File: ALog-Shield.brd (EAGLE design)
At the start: 53.3 x 78.5 mm, 29 parts, among them U1 DS3231MZ/V+T

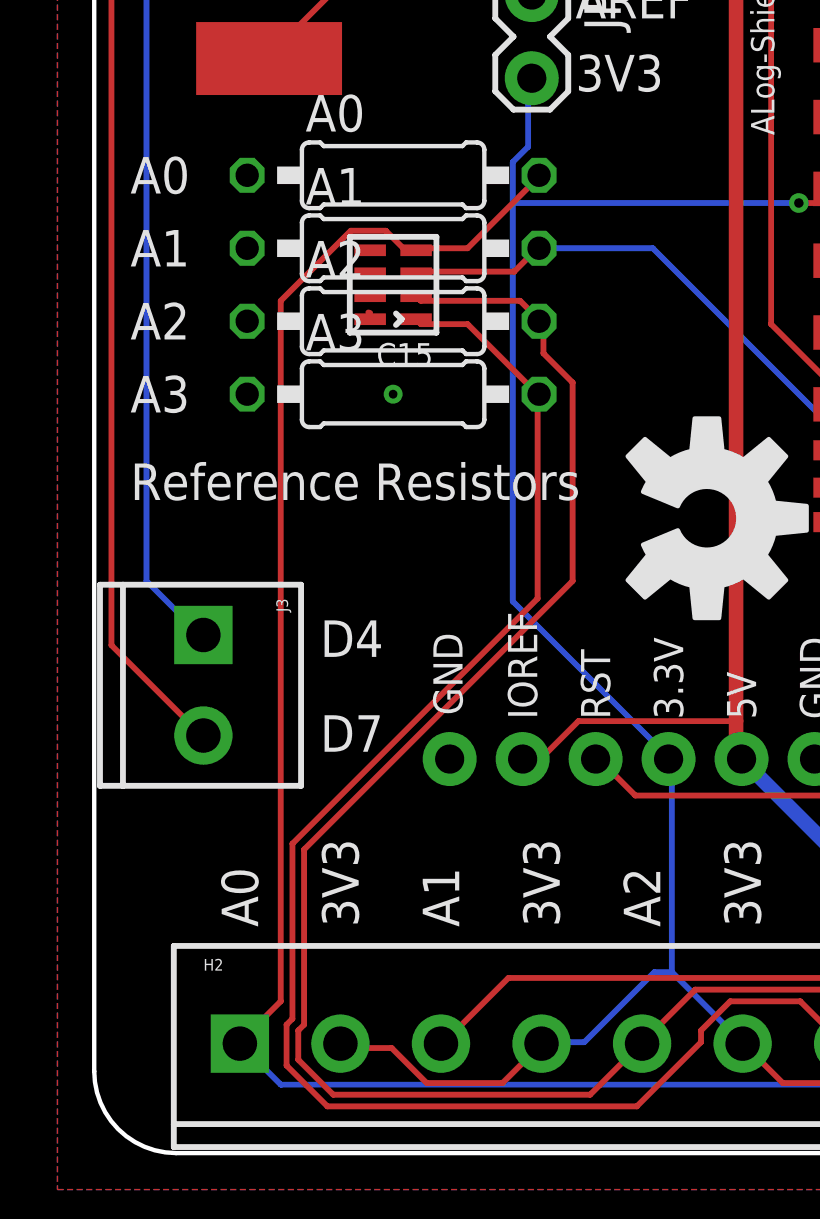
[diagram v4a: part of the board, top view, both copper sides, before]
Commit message: rm cap array
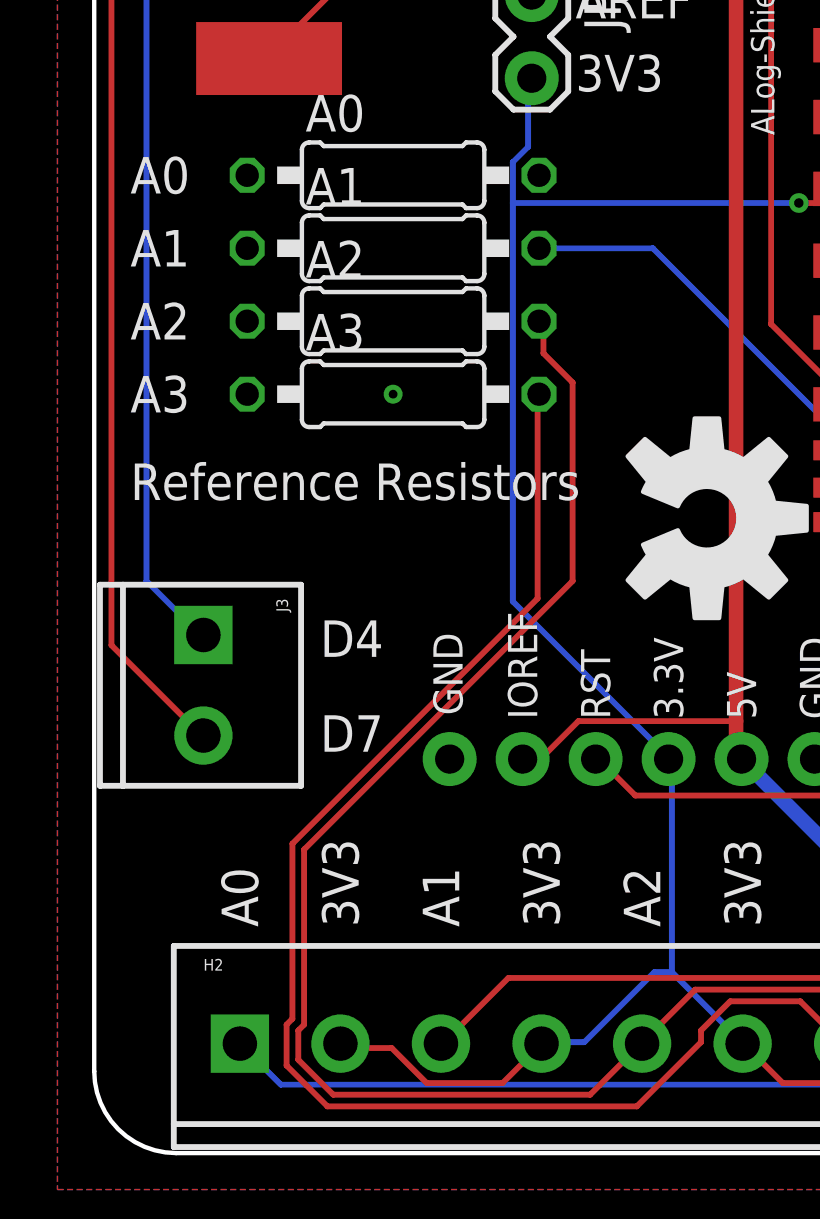
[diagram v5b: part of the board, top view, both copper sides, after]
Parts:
- removed C15: 10nF, rc-master-smd:CECJ-CTS-031817
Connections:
- net A0: no longer C15.D1
- net A1: no longer C15.C1
- net A2: no longer C15.B1
- net A3: no longer C15.A1
- net GND: no longer C15.A2, C15.B2, C15.C2, C15.D2
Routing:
- net A0: track 79.3 -> 41.4 mm
- net A3: track 75.5 -> 70.2 mm
- net A2: track 73.4 -> 68.7 mm
- net A1: track 64.1 -> 59.5 mm
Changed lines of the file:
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@@
 <attribute name="SF_ID" value="2xPRT-08084" x="33.08" y="74.676" size="1.778" layer="27" display="off"/>
 </element>
-<element name="C15" library="rc-master-smd" package="CECJ-CTS-031817" value="10nF" x="10.414" y="30.226" rot="R90"/>
 <element name="CLOCK_BATT" library="awickert" package="LINX_BAT-HLD-012-SMT" value="Linx BAT-HLD-012-SMT" x="6.096" y="45.72" rot="R90"/>
 <element name="U$2" library="awickert" package="MADE_IN_MN_SHIELD_220" value="MADE_IN_MN_220_SHIELD" x="42.926" y="30.48" rot="R90"/>
@@
 </polygon>
 <via x="27.432" y="48.26" extent="1-16" drill="0.3048" shape="octagon"/>
-<contactref element="C15" pad="D2"/>
-<contactref element="C15" pad="C2"/>
-<contactref element="C15" pad="B2"/>
-<contactref element="C15" pad="A2"/>
 <via x="10.414" y="26.416" extent="1-16" drill="0.3048" shape="octagon"/>
 <contactref element="CLOCK_BATT" pad="GND"/>
-<wire x1="9.5504" y1="29.2608" x2="9.6140125" y2="29.2418" width="0.2032" layer="1"/>
 <contactref element="CLK_DECOUP" pad="2"/>
 <via x="33.782" y="48.26" extent="1-16" drill="0.3048" shape="octagon"/>
+<wire x1="33.08" y1="74.676" x2="50.422" y2="75.735" width="0" layer="19" extent="1-1"/>
+<wire x1="29.591" y1="56.7944" x2="33.08" y2="74.676" width="0" layer="19" extent="1-1"/>
+<wire x1="25.284" y1="55.626" x2="29.591" y2="56.7944" width="0" layer="19" extent="1-1"/>
+<wire x1="25.234" y1="53.721" x2="25.284" y2="55.626" width="0" layer="19" extent="1-1"/>
+<wire x1="29.591" y1="50.6476" x2="25.234" y2="53.721" width="0" layer="19" extent="1-1"/>
+<wire x1="32.131" y1="50.6476" x2="29.591" y2="50.6476" width="0" layer="19" extent="1-1"/>
+<wire x1="33.782" y1="48.26" x2="32.131" y2="50.6476" width="0" layer="19" extent="1-1"/>
+<wire x1="35.941" y1="50.6476" x2="33.782" y2="48.26" width="0" layer="19" extent="1-1"/>
+<wire x1="27.432" y1="48.26" x2="29.591" y2="50.6476" width="0" layer="19" extent="1-1"/>
+<wire x1="28.84" y1="45.863" x2="27.432" y2="48.26" width="0" layer="19" extent="1-1"/>
+<wire x1="18.669" y1="51.3588" x2="25.234" y2="53.721" width="0" layer="19" extent="1-1"/>
+<wire x1="27.04" y1="36.063" x2="28.84" y2="45.863" width="0" layer="19" extent="1-1"/>
+<wire x1="27.04" y1="28.563" x2="27.04" y2="36.063" width="0" layer="19" extent="1-1"/>
+<wire x1="11.1125" y1="61.976" x2="18.669" y2="51.3588" width="0" layer="19" extent="1-1"/>
+<wire x1="48.109" y1="56.007" x2="35.941" y2="50.6476" width="0" layer="19" extent="1-1"/>
+<wire x1="6.096" y1="45.72" x2="18.669" y2="51.3588" width="0" layer="19" extent="1-1"/>
+<wire x1="5.334" y1="34.036" x2="6.096" y2="45.72" width="0" layer="19" extent="1-1"/>
+<wire x1="5.334" y1="31.496" x2="5.334" y2="34.036" width="0" layer="19" extent="1-1"/>
+<wire x1="5.334" y1="28.956" x2="5.334" y2="31.496" width="0" layer="19" extent="1-1"/>
+<wire x1="5.334" y1="26.416" x2="5.334" y2="28.956" width="0" layer="19" extent="1-1"/>
+<wire x1="10.414" y1="26.416" x2="5.334" y2="26.416" width="0" layer="19" extent="1-1"/>
+<wire x1="12.3825" y1="13.716" x2="10.414" y2="26.416" width="0" layer="19" extent="1-1"/>
+<wire x1="25.0825" y1="13.716" x2="12.3825" y2="13.716" width="0" layer="19" extent="1-1"/>
+<wire x1="27.6225" y1="13.716" x2="25.0825" y2="13.716" width="0" layer="19" extent="1-1"/>
+<wire x1="36.58" y1="3.81" x2="27.6225" y2="13.716" width="0" layer="19" extent="1-1"/>
+<wire x1="47.622" y1="2.497" x2="36.58" y2="3.81" width="0" layer="19" extent="1-1"/>
+<wire x1="5.08" y1="74.676" x2="11.1125" y2="61.976" width="0" layer="19" extent="1-1"/>
+<wire x1="49.74" y1="20.363" x2="47.622" y2="2.497" width="0" layer="19" extent="1-1"/>
 </signal>
 <signal name="VCC">
@@
 <wire x1="19.1008" y1="3.8608" x2="19.08" y2="3.81" width="0.2032" layer="1"/>
 <contactref element="A2" pad="2"/>
-<contactref element="C15" pad="B1"/>
-<wire x1="14.8336" y1="29.6672" x2="11.3792" y2="29.6672" width="0.2032" layer="1"/>
-<wire x1="15.4432" y1="29.0576" x2="14.8336" y2="29.6672" width="0.2032" layer="1"/>
-<wire x1="11.3792" y1="29.6672" x2="11.214" y2="29.826" width="0.2032" layer="1"/>
-<wire x1="15.4432" y1="29.0576" x2="15.494" y2="28.956" width="0.2032" layer="1"/>
 <wire x1="15.6464" y1="27.8384" x2="15.6464" y2="28.8544" width="0.2032" layer="1"/>
 <wire x1="16.6624" y1="26.8224" x2="15.6464" y2="27.8384" width="0.2032" layer="1"/>
@@
 <wire x1="5.08" y1="3.81" x2="6.50875" y2="2.38125" width="0.2032" layer="16"/>
 <contactref element="A0" pad="2"/>
-<contactref element="C15" pad="D1"/>
-<wire x1="13.0048" y1="31.496" x2="11.3792" y2="31.496" width="0.2032" layer="1"/>
-<wire x1="15.4432" y1="33.9344" x2="13.0048" y2="31.496" width="0.2032" layer="1"/>
-<wire x1="11.3792" y1="31.496" x2="11.214" y2="31.426" width="0.2032" layer="1"/>
-<wire x1="15.4432" y1="33.9344" x2="15.494" y2="34.036" width="0.2032" layer="1"/>
-<wire x1="10.7696" y1="31.496" x2="11.176" y2="31.496" width="0.2032" layer="1"/>
-<wire x1="10.16" y1="32.1056" x2="10.7696" y2="31.496" width="0.2032" layer="1"/>
-<wire x1="8.9408" y1="32.1056" x2="10.16" y2="32.1056" width="0.2032" layer="1"/>
-<wire x1="6.5024" y1="29.6672" x2="8.9408" y2="32.1056" width="0.2032" layer="1"/>
-<wire x1="6.5024" y1="5.2832" x2="6.5024" y2="29.6672" width="0.2032" layer="1"/>
-<wire x1="5.08" y1="3.8608" x2="6.5024" y2="5.2832" width="0.2032" layer="1"/>
-<wire x1="11.176" y1="31.496" x2="11.214" y2="31.426" width="0.2032" layer="1"/>
-<wire x1="5.08" y1="3.8608" x2="5.08" y2="3.81" width="0.2032" layer="1"/>
+<wire x1="35.2425" y1="13.716" x2="15.494" y2="34.036" width="0" layer="19" extent="1-1"/>
 </signal>
 <signal name="A3">
@@
 <wire x1="42.672" y1="13.6144" x2="42.8625" y2="13.716" width="0.2032" layer="1"/>
 <wire x1="26.2128" y1="3.8608" x2="26.08" y2="3.81" width="0.2032" layer="1"/>
-<contactref element="C15" pad="A1"/>
 <contactref element="A3" pad="2"/>
-<wire x1="13.0048" y1="28.8544" x2="11.3792" y2="28.8544" width="0.2032" layer="1"/>
-<wire x1="15.4432" y1="26.416" x2="13.0048" y2="28.8544" width="0.2032" layer="1"/>
-<wire x1="11.3792" y1="28.8544" x2="11.214" y2="29.026" width="0.2032" layer="1"/>
 <wire x1="15.4432" y1="19.304" x2="15.4432" y2="26.416" width="0.2032" layer="1"/>
 <wire x1="6.9088" y1="10.7696" x2="15.4432" y2="19.304" width="0.2032" layer="1"/>
@@
 <wire x1="12.192" y1="3.8608" x2="12.08" y2="3.81" width="0.2032" layer="1"/>
 <contactref element="A1" pad="2"/>
-<contactref element="C15" pad="C1"/>
-<wire x1="14.6304" y1="30.6832" x2="11.3792" y2="30.6832" width="0.2032" layer="1"/>
-<wire x1="15.4432" y1="31.496" x2="14.6304" y2="30.6832" width="0.2032" layer="1"/>
-<wire x1="11.3792" y1="30.6832" x2="11.214" y2="30.626" width="0.2032" layer="1"/>
-<wire x1="15.4432" y1="31.496" x2="15.494" y2="31.496" width="0.2032" layer="1"/>
 <wire x1="19.4564" y1="31.496" x2="15.494" y2="31.496" width="0.2032" layer="16"/>
 <wire x1="37.338" y1="13.6144" x2="19.4564" y2="31.496" width="0.2032" layer="16"/>

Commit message: Bobby's caps
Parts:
- added C1, C2, C3, C4: (no value), bschulz_passives:C0603
- CLK_DECOUP: device SparkFun-Passives:0805 -> bschulz_passives:C0805
- CLOCK_BATT_DECOUP: device rcl:C0603 -> bschulz_passives:C0603
- R_PU_A, R_PU_L: device resistor:R0603 -> bschulz_passives:R0603
- moved CLK_DECOUP 0.25 mm to (24.4, 55.9)
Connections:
- net A0: now also C1.1
- net A1: now also C2.1
- net A2: now also C3.1
- net A3: now also C4.1
- net GND: now also C1.2, C2.2, C3.2, C4.2
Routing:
- net BAT: track 37.2 -> 28.0 mm
- net VCC: track 107.5 -> 98.7 mm

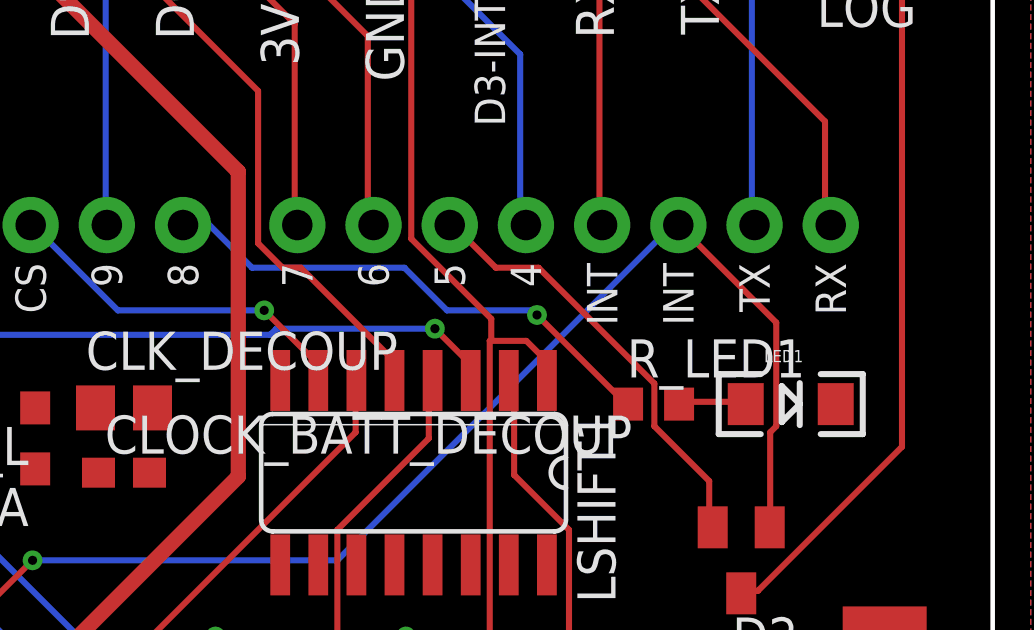
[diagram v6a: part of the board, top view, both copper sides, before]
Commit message: R220K to R330K ColdSilicon
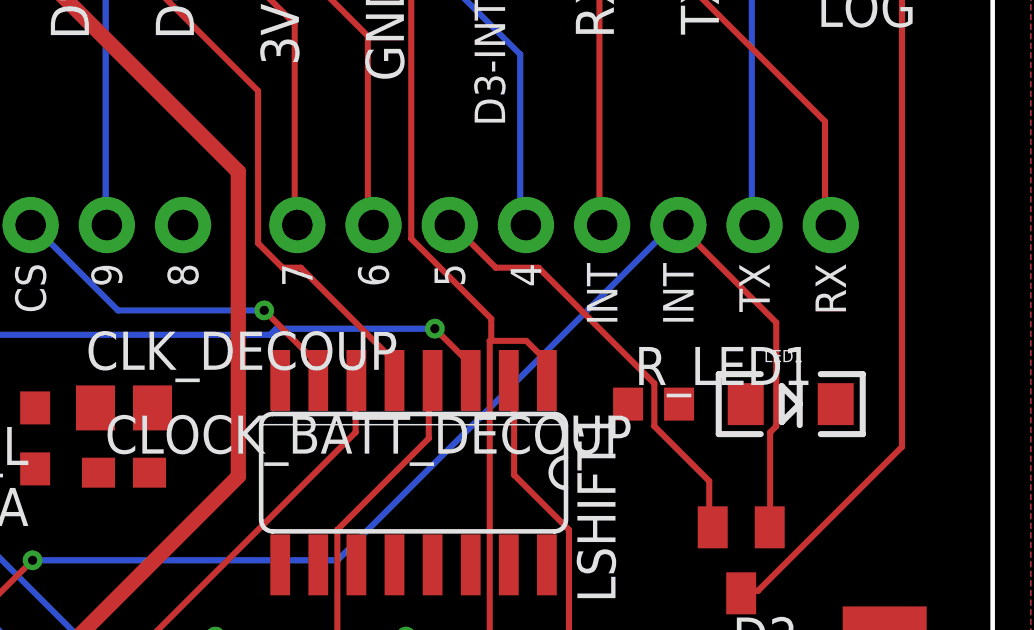
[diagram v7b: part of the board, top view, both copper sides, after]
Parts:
- R_LED1: device resistor:R0603 -> bschulz_passives:R0603
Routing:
- net D8-EXT: track 17.3 -> 0.00 mm, vias 1 -> 0
- net LED+1: track 2.25 -> 0.00 mm
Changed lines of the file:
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@@
 <element name="A3" library="resistor" package="0207/10" value="" x="10.414" y="26.416"/>
 <element name="LED1" library="SparkFun-LED" package="LED-1206" value="" x="46.609" y="56.007"/>
-<element name="R_LED1" library="resistor" package="R0603" value="220" x="42.037" y="56.007"/>
+<element name="R_LED1" library="bschulz_passives" package="R0603" value="220" x="42.037" y="56.007">
+<attribute name="DIGIKEY" value="311-330HRCT-ND" x="42.037" y="56.007" size="1.778" layer="27" display="off"/>
+<attribute name="MF" value="Yageo" x="42.037" y="56.007" size="1.778" layer="27" display="off"/>
+<attribute name="MPN" value="RC0603FR-07330RL" x="42.037" y="56.007" size="1.778" layer="27" display="off"/>
+<attribute name="VALUE_PART" value="330" x="42.037" y="56.007" size="1.778" layer="27" display="off"/>
+</element>
 <element name="A1" library="resistor" package="0207/10" value="" x="10.414" y="31.496"/>
 <element name="RESET" library="bschulz" package="SWITCH_4.2X3.2" value="Reset" x="49.022" y="4.572" smashed="yes" rot="R90">
@@
 <contactref element="LED1" pad="A"/>
 <contactref element="R_LED1" pad="2"/>
-<wire x1="44.9072" y1="56.0832" x2="43.0784" y2="56.0832" width="0.2032" layer="1"/>
-<wire x1="43.0784" y1="56.0832" x2="42.887" y2="56.007" width="0.2032" layer="1"/>
-<wire x1="44.9072" y1="56.0832" x2="45.109" y2="56.007" width="0.2032" layer="1"/>
+<wire x1="42.887" y1="56.007" x2="45.109" y2="56.007" width="0" layer="19" extent="1-1"/>
 </signal>
 <signal name="N$11">
@@
 <contactref element="U$9" pad="D8"/>
 <contactref element="R_LED1" pad="1"/>
-<wire x1="41.0464" y1="56.0832" x2="41.187" y2="56.007" width="0.2032" layer="1"/>
-<wire x1="38.1508" y1="58.9788" x2="41.0464" y2="56.0832" width="0.2032" layer="1"/>
-<via x="38.1508" y="58.9788" extent="1-16" drill="0.3048"/>
-<wire x1="35.1536" y1="59.1312" x2="37.9984" y2="59.1312" width="0.2032" layer="16"/>
-<wire x1="33.7312" y1="60.5536" x2="35.1536" y2="59.1312" width="0.2032" layer="16"/>
-<wire x1="28.6512" y1="60.5536" x2="33.7312" y2="60.5536" width="0.2032" layer="16"/>
-<wire x1="27.2288" y1="61.976" x2="28.6512" y2="60.5536" width="0.2032" layer="16"/>
-<wire x1="37.9984" y1="59.1312" x2="38.1508" y2="58.9788" width="0.2032" layer="16"/>
-<wire x1="27.2288" y1="61.976" x2="26.3525" y2="61.976" width="0.2032" layer="16"/>
+<wire x1="26.3525" y1="61.976" x2="41.187" y2="56.007" width="0" layer="19" extent="1-1"/>
 </signal>
 <signal name="D9-CS-EXT">

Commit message: ColdSilicon DS3231M
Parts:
- removed U1: DS3231MZ/V+T, Maxim-DS3231MZ_8-SOIC:21-0041B_8
- added RTC1: DS3231M, bschulz:SO08
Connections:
- net BAT: now also RTC1.6; no longer U1.6
- net GND: now also RTC1.5; no longer U1.5
- net INT0: now also RTC1.3; no longer U1.3
- net SCL: now also RTC1.8; no longer U1.8
- net SDA: now also RTC1.7; no longer U1.7
- net VCC: now also RTC1.2; no longer U1.2
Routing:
- net A0: track 41.4 -> 79.0 mm
- net D8-EXT: track 0.00 -> 17.3 mm, vias 0 -> 1
- net SDA: track 99.9 -> 84.3 mm, vias 0 -> 1
- net BAT: track 28.0 -> 40.8 mm
- net VCC: track 98.7 -> 105.4 mm
- net A3: track 70.2 -> 74.0 mm, vias 0 -> 1
- net SCL: track 108.0 -> 104.7 mm
- net A1: track 59.5 -> 62.5 mm
- net A2: track 68.7 -> 71.5 mm
- net LED+1: track 0.00 -> 2.22 mm
